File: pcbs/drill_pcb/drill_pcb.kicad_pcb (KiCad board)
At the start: 2 copper layers, 25 parts, among them J1 WEIGHT SENSOR, J10 DC MOTOR UART, J11 motor1, J12 motor2, J2 DC MOTOR 24 V, J3 LIMIT SENSOR TOP, J4 LIMIT SENSOR BOTTOM, J5 ENCODER VERTICAL DRIVE, J6 ENCODER STORAGE, J7 HEIGHT SENSOR, J8 STEPPER VERTICAL DRIVE, J9 STEPPER STORAGE, U101 TXS0108EPW, U102 ESP32-DevKitC

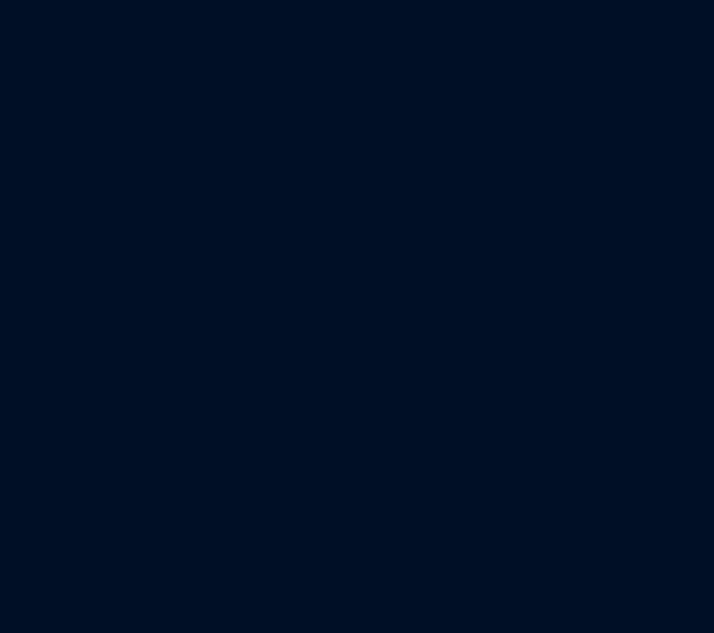
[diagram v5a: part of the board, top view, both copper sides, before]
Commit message: driver pin update
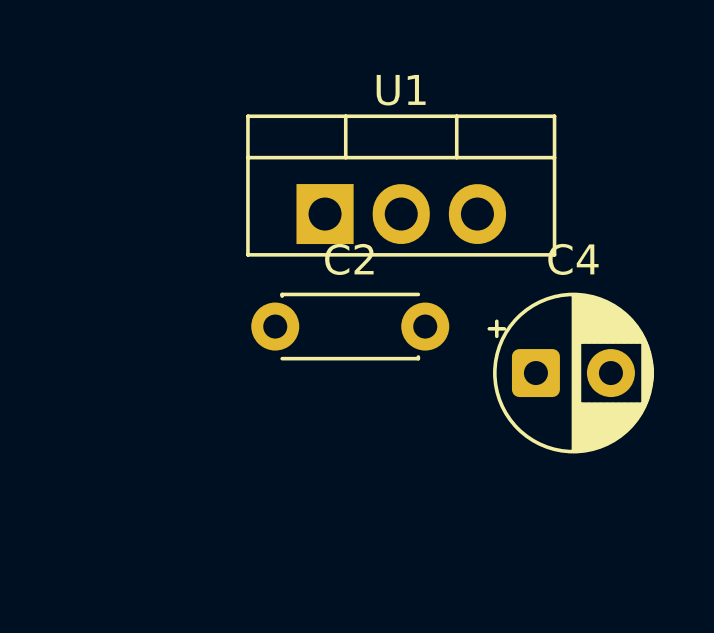
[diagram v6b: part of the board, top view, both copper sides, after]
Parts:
- added C2: 0,47 μF, Capacitor_THT:C_Disc_D4.3mm_W1.9mm_P5.00mm, F.Cu at (259.1, 52.7)
- added C4: 33 μF, Capacitor_THT:CP_Radial_D5.0mm_P2.50mm, F.Cu at (267.8, 54.2)
- added U1: LM3940, Package_TO_SOT_THT:TO-220-3_Vertical, F.Cu at (260.7, 49.0)
- A1: value Driver_TMC2209 -> Driver_TMC2208
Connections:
- net EN1 renamed ENABLE1
- A1 pad 10: 5V -> +3.3V
- A1 pad 16: 24V -> +24V
- A1 pad 17: (no net) -> DIAG01
- A1 pad 18: (no net) -> GIAG11
- A1 pad 4: RX -> unconnected-(A1-RX-Pad4)
- A1 pad 6: unconnected-(A1-CLK-Pad6) -> CLK1
- A2 pad 1: EN2 -> ENABLE2
- A2 pad 10: 5V -> +3.3V
- A2 pad 16: 24V -> +24V
- A2 pad 17: (no net) -> DIAG02
- A2 pad 18: (no net) -> GIAG12
- A2 pad 2: 5V -> MOSI
- A2 pad 3: unconnected-(A2-MS2-Pad3) -> SCK
- A2 pad 4: RX -> CS
- A2 pad 5: unconnected-(A2-TX-Pad5) -> MISO
- A2 pad 6: unconnected-(A2-CLK-Pad6) -> CLK2
- C5 pad 1: 24V -> +24V
- C6 pad 1: 24V -> +24V
- U102 pad 10: unconnected-(U102-DAC_2/ADC2_CH9/GPIO26-Pad10) -> DIR2
- U102 pad 11: unconnected-(U102-ADC2_CH7/GPIO27-Pad11) -> ENABLE2
- U102 pad 30: unconnected-(U102-GPIO18-Pad30) -> STEP2
- U102 pad 5: unconnected-(U102-VDET_1/GPIO34/ADC1_CH6-Pad5) -> DIAG02
- U102 pad 6: unconnected-(U102-VDET_2/GPIO35/ADC1_CH7-Pad6) -> GIAG12
- U102 pad 9: unconnected-(U102-DAC_1/ADC2_CH8/GPIO25-Pad9) -> STEP2

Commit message: Further work on the PCB. Schematic complete AFAIK. Routing in progress.
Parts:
- removed C102, C103: 100n, Capacitor_SMD:C_1206_3216Metric_Pad1.33x1.80mm_HandSolder
- removed the C2 at (259.1, 52.7)
- removed the J1 at (112.5, 68.8)
- removed the J4 at (112.5, 99.8)
- removed the J8 at (98.0, 92.2)
- removed U101: TXS0108EPW, Package_SO:TSSOP-20_4.4x6.5mm_P0.65mm
- added C1: 33 μF, Capacitor_THT:CP_Radial_D5.0mm_P2.50mm, F.Cu at (53.7, 43.9)
- added C4: 100n, Capacitor_SMD:C_1206_3216Metric_Pad1.33x1.80mm_HandSolder, F.Cu at (60.9, 59.1)
- added J3: DC MOTOR UART, Connector_JST:JST_XH_B3B-XH-A_1x03_P2.50mm_Vertical, F.Cu at (109.2, 36.3)
- added R1: 1k, Resistor_SMD:R_1206_3216Metric, F.Cu at (90.3, 94.7)
- added REF**: MountingHole_3.2mm_M3, MountingHole:MountingHole_3.2mm_M3, F.Cu at (35.0, 137.0)
- added REF**: MountingHole_3.2mm_M3, MountingHole:MountingHole_3.2mm_M3, F.Cu at (35.0, 35.0)
- J10: value DC MOTOR UART -> WEIGHT SENSOR; footprint drill_T-DEAN:DEANS -> Connector_JST:JST_XH_B7B-XH-A_1x07_P2.50mm_Vertical
- J11: value motor1 -> STEPPER STORAGE
- J7: renamed from J12; value motor2 -> STEPPER VERTICAL DRIVE
- J9: value STEPPER STORAGE -> LIMIT SENSOR BOTTOM; footprint Connector_JST:JST_XH_B4B-XH-A_1x04_P2.50mm_Vertical -> Connector_JST:JST_XH_B3B-XH-A_1x03_P2.50mm_Vertical
- moved U2 205.0 mm to (55.8, 54.3)
- moved C3 204.6 mm to (63.4, 43.9), turned to 180 degrees
- moved U1 159.4 mm to (73.6, 89.6), turned to 90 degrees
- moved J11 143.7 mm to (86.2, 130.3), turned to 180 degrees
- moved V1 131.5 mm to (44.6, 82.3)
- moved F1 130.7 mm to (37.6, 123.0)
- moved A2 130.1 mm to (91.4, 109.9), turned to -90 degrees
- moved F2 125.9 mm to (46.6, 123.4)
- moved J1 125.9 mm to (51.1, 134.9)
- moved C2 125.9 mm to (50.7, 61.4)
- moved C6 123.6 mm to (97.0, 128.9), turned to -90 degrees
- moved A1 117.9 mm to (121.9, 109.9), turned to -90 degrees
- moved J7 112.7 mm to (116.7, 130.3), turned to 180 degrees
- moved C5 92.5 mm to (126.9, 128.7), turned to -90 degrees
- moved J10 82.7 mm to (53.3, 36.3)
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- renumbered A2 to A1, A1 to A2, C101 to C2, C4 to C3, C6 to C5, C5 to C6, F101 to F1, F102 to F2, Dean101 to J1, J5 to J4, J3 to J5, J7 to J6, J6 to J8, U102 to U1, U1 to U2, V101 to V1
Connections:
- net DIAG02 renamed DRVR_VERT_DIAG0
- net DIR2 renamed DRVR_VERT_DIR
- net ENABLE2 renamed DRVR_VERT_ENABLE
- net GIAG12 renamed DRVR_VERT_DIAG1
- A1 pad 2: MOSI -> VSPI_MOSI
- A1 pad 3: SCK -> VSPI_SCK
- A1 pad 4: CS -> VSPI_CS1
- A1 pad 5: MISO -> VSPI_MISO
- A1 pad 6: CLK2 -> unconnected-(A1-CLK-Pad6)
- A1 pad 7: STEP2 -> DRVR_VERT_STEP
- A2 pad 1: ENABLE1 -> DRVR_STORAGE_ENABLE
- A2 pad 17: DIAG01 -> DRVR_STORAGE_0
- A2 pad 18: GIAG11 -> DRVR_STORAGE_1
- A2 pad 4: unconnected-(A1-RX-Pad4) -> RX1
- A2 pad 6: CLK1 -> unconnected-(A2-CLK-Pad6)
- A2 pad 7: STEP1 -> DRVR_STORAGE_STEP
- A2 pad 8: DIR1 -> DRVR_STORAGE_DIR
- C3 pad 1: Net-(U1-VO) -> +3.3V
- J10 pad 1: TX2 -> +5V
- J10 pad 2: RX2 -> +3.3V
- J9 pad 1: unconnected-(J9-Pin_1-Pad1) -> +3.3V
- J9 pad 2: unconnected-(J9-Pin_2-Pad2) -> LIMIT_SENSOR_BOTTOM
- J9 pad 3: unconnected-(J9-Pin_3-Pad3) -> GND
- U1 pad 1: unconnected-(U102-3V3-Pad1) -> +3.3V
- U1 pad 12: unconnected-(U102-MTMS/GPIO14/ADC2_CH6-Pad12) -> DRVR_STORAGE_ENABLE
- U1 pad 13: unconnected-(U102-MTDI/GPIO12/ADC2_CH5-Pad13) -> DRVR_STORAGE_DIR
- U1 pad 15: unconnected-(U102-MTCK/GPIO13/ADC2_CH4-Pad15) -> DRVR_STORAGE_STEP
- U1 pad 23: unconnected-(U102-MTDO/GPIO15/ADC2_CH3-Pad23) -> LIMIT_SENSOR_BOTTOM
- U1 pad 24: unconnected-(U102-ADC2_CH2/GPIO2-Pad24) -> ADC_RST
- U1 pad 25: unconnected-(U102-GPIO0/BOOT/ADC2_CH1-Pad25) -> LIMIT_SENSOR_TOP
- U1 pad 26: unconnected-(U102-ADC2_CH0/GPIO4-Pad26) -> ADC_DRDY
- U1 pad 27: unconnected-(U102-GPIO16-Pad27) -> RX2
- U1 pad 28: unconnected-(U102-GPIO17-Pad28) -> TX2
- U1 pad 29: unconnected-(U102-GPIO5-Pad29) -> VSPI_CS1
- U1 pad 3: unconnected-(U102-SENSOR_VP/GPIO36/ADC1_CH0-Pad3) -> DRVR_STORAGE_0
- U1 pad 30: STEP2 -> VSPI_SCK
- U1 pad 31: unconnected-(U102-GPIO19-Pad31) -> VSPI_MISO
- U1 pad 33: unconnected-(U102-GPIO21-Pad33) -> SDA1
- U1 pad 36: unconnected-(U102-GPIO22-Pad36) -> SCL1
- U1 pad 37: unconnected-(U102-GPIO23-Pad37) -> VSPI_MOSI
- U1 pad 4: unconnected-(U102-SENSOR_VN/GPIO39/ADC1_CH3-Pad4) -> DRVR_STORAGE_1
- U1 pad 7: unconnected-(U102-32K_XP/GPIO32/ADC1_CH4-Pad7) -> RX1
- U1 pad 8: unconnected-(U102-32K_XN/GPIO33/ADC1_CH5-Pad8) -> Net-(U1-32K_XN/GPIO33/ADC1_CH5)
- U1 pad 9: STEP2 -> DRVR_VERT_STEP
- U2 pad 1: Net-(U1-VI) -> +5V
- U2 pad 3: Net-(U1-VO) -> +3.3V
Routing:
- net GND: track 89.6 -> 416.0 mm
- net +3.3V: track 0.00 -> 208.1 mm
- net +24V: track 40.4 -> 117.6 mm
- net DRVR_VERT_DIAG0: track 0.00 -> 57.4 mm
- net DRVR_STORAGE_0: track 0.00 -> 56.9 mm
- net ADC_RST: track 0.00 -> 55.0 mm
- net SDA1: track 0.00 -> 54.8 mm
- net ADC_DRDY: track 0.00 -> 52.4 mm
- net SCL1: track 0.00 -> 49.9 mm
- net DRVR_VERT_DIAG1: track 0.00 -> 49.1 mm
- net +5V: track 7.68 -> 55.8 mm
- net DRVR_STORAGE_1: track 0.00 -> 45.8 mm
- net TX2: track 0.00 -> 35.3 mm
- net DRVR_VERT_STEP: track 0.00 -> 29.6 mm
- net RX2: track 0.00 -> 29.0 mm
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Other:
- board outline added: 109 x 112 mm

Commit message: PCB should be fully complete now. Somebody pls review it :(
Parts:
- removed the REF** at (35.0, 137.0)
- removed the REF** at (35.0, 35.0)
- added G***: LOGO, logo:logo, F.Cu at (62.2, 106.7)
- added REF**: MountingHole_3.2mm_M3, MountingHole:MountingHole_3.2mm_M3, F.Cu at (35.0, 45.0)
- added REF**: MountingHole_3.2mm_M3, MountingHole:MountingHole_3.2mm_M3, F.Cu at (35.0, 138.0)
- added REF**: MountingHole_3.2mm_M3, MountingHole:MountingHole_3.2mm_M3, F.Cu at (130.0, 138.0)
- added REF**: MountingHole_3.2mm_M3, MountingHole:MountingHole_3.2mm_M3, F.Cu at (130.0, 45.0)
- C2: moved to F.Cu
- moved C1 17.5 mm to (40.6, 55.6), turned to -90 degrees
- moved J5 15.0 mm to (104.1, 59.7)
- moved R1 14.5 mm to (90.2, 109.2)
- moved J9 14.5 mm to (104.1, 68.6)
- moved J3 14.5 mm to (109.2, 50.8)
- moved J6 14.5 mm to (86.3, 50.8)
- moved J8 13.3 mm to (86.4, 59.7)
- moved U1 13.2 mm to (73.6, 102.9)
- moved C3 12.3 mm to (67.3, 55.6), turned to -90 degrees
- moved J4 11.9 mm to (86.3, 68.6)
- moved F2 11.1 mm to (35.6, 123.6)
- moved J10 9.44 mm to (53.3, 45.7)
- moved F1 9.37 mm to (47.0, 123.6)
- moved C5 9.07 mm to (120.0, 134.5)
- moved A1 7.65 mm to (115.6, 114.3)
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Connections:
- F2 pad 1: +24V -> Net-(J1-Pin_1)
- U1 pad 10: DRVR_VERT_DIR -> DRVR_STORAGE_STEP
- U1 pad 11: DRVR_VERT_ENABLE -> DRVR_STORAGE_ENABLE
- U1 pad 12: DRVR_STORAGE_ENABLE -> DRVR_VERT_ENABLE
- U1 pad 13: DRVR_STORAGE_DIR -> DRVR_VERT_DIR
- U1 pad 15: DRVR_STORAGE_STEP -> DRVR_VERT_STEP
- U1 pad 23: LIMIT_SENSOR_BOTTOM -> LIMIT_SENSOR_TOP
- U1 pad 25: LIMIT_SENSOR_TOP -> LIMIT_SENSOR_BOTTOM
- U1 pad 3: DRVR_STORAGE_0 -> DRVR_VERT_DIAG1
- U1 pad 4: DRVR_STORAGE_1 -> DRVR_VERT_DIAG0
- U1 pad 5: DRVR_VERT_DIAG0 -> DRVR_STORAGE_1
- U1 pad 6: DRVR_VERT_DIAG1 -> DRVR_STORAGE_0
- U1 pad 9: DRVR_VERT_STEP -> DRVR_STORAGE_DIR
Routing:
- net GND: track 416.0 -> 16.6 mm
- net VSPI_MOSI: track 0.00 -> 82.5 mm
- net VSPI_MISO: track 0.00 -> 74.6 mm
- net VSPI_CS1: track 0.00 -> 72.3 mm
- net VSPI_SCK: track 0.00 -> 68.0 mm
- net DRVR_VERT_ENABLE: track 0.00 -> 37.2 mm
- net +3.3V: track 208.1 -> 244.1 mm
- net DRVR_STORAGE_DIR: track 0.00 -> 28.7 mm
- net DRVR_STORAGE_STEP: track 0.00 -> 28.7 mm
- net DRVR_VERT_DIAG1: track 49.1 -> 73.7 mm
- net +24V: track 117.6 -> 93.6 mm
- net +5V: track 55.8 -> 32.0 mm
- net DRVR_VERT_DIAG0: track 57.4 -> 74.0 mm
- net DRVR_STORAGE_ENABLE: track 0.00 -> 14.6 mm
- net DRVR_VERT_STEP: track 29.6 -> 15.1 mm
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- added copper zone on B.Cu, net GND
- added copper zone on F.Cu, net GND
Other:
- board size 109 x 112 mm -> 105 x 103 mm
